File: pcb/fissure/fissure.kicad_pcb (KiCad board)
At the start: 2 copper layers, 99.5 x 95 mm, 45 parts, among them J1 AudioJack4, J2 AudioJack4, K1 KEYSW, K10 KEYSW, K11 KEYSW, K12 KEYSW, K13 KEYSW, K14 KEYSW, K15 KEYSW, K16 KEYSW, K17 KEYSW, K18 KEYSW, K2 KEYSW, K3 KEYSW, K4 KEYSW, K5 KEYSW, K6 KEYSW, K7 KEYSW, K8 KEYSW, K9 KEYSW, SW1 SW_PUSH, U1 NRF24L01_Breakout, U3 ProMicro

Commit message: v2.1 final
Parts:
- removed U1: NRF24L01_Breakout, Connector_PinHeader_2.54mm:PinHeader_2x04_P2.54mm_Vertical
- added J3: joystick, footprints:joystick, B.Cu at (102.5, 120.2)
- added J4: joystick, footprints:joystick, F.Cu at (102.5, 120.2)
- J1, J2: footprint Keebio-Parts:TRRS-PJ-320A -> Keebio-Parts:TRRS-PJ-320D
- moved R2 72.9 mm to (59.5, 44.7), turned to 270 degrees
- moved R1 68.8 mm to (62.5, 44.7), turned to 270 degrees
- moved D15 9.71 mm to (96.5, 53.2)
- moved D14 9.31 mm to (88.5, 53.2)
- moved D17 7.42 mm to (92.5, 53.2)
- moved SW1 6.75 mm to (113.0, 54.2)
- moved D18 5.82 mm to (102.5, 53.2)
- moved D10 5.62 mm to (98.5, 53.2)
- moved D9 5.22 mm to (90.5, 53.2)
- moved D16 5.02 mm to (86.5, 53.2)
- moved D13 4.93 mm to (84.5, 53.2)
- moved D8 4.83 mm to (82.5, 53.2)
- moved D3 4.73 mm to (80.5, 53.2)
- moved K1 2.50 mm to (51.5, 87.2)
- moved K11 2.50 mm to (54.5, 121.2)
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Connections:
- U3 pad 1: TX -> COL1
- U3 pad 10: COL4 -> ROW4
- U3 pad 11: COL5 -> X
- U3 pad 12: RGB -> Y
- U3 pad 13: CS -> RGB
- U3 pad 14: MOSI -> COL5
- U3 pad 15: MISO -> COL4
- U3 pad 16: SCLK -> COL3
- U3 pad 17: ROW4 -> Net-(U3-Pad17)
- U3 pad 18: ROW3 -> Net-(U3-Pad18)
- U3 pad 19: ROW2 -> Net-(U3-Pad19)
- U3 pad 2: RX -> COL2
- U3 pad 20: ROW1 -> Net-(U3-Pad20)
- U3 pad 7: COL1 -> ROW1
- U3 pad 8: COL2 -> ROW2
- U3 pad 9: COL3 -> ROW3
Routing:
- net Y: track 0.00 -> 76.7 mm
- net X: track 0.00 -> 73.6 mm
- net SCLK: track 69.9 -> 0.00 mm
- net MISO: track 63.2 -> 0.00 mm
- net MOSI: track 59.7 -> 0.00 mm
- net CS: track 59.7 -> 0.00 mm
- net ROW3: track 181.1 -> 130.7 mm
- net ROW4: track 169.8 -> 120.5 mm
- net ROW1: track 140.6 -> 95.0 mm
- net GND: track 176.4 -> 221.9 mm, vias 0 -> 1
- net ROW2: track 159.5 -> 115.0 mm
- net RGB: track 111.7 -> 131.6 mm, vias 2 -> 1
- net COL1: track 18.2 -> 7.83 mm
- net Net-(D16-Pad1): track 79.3 -> 88.7 mm
- net COL5: track 38.0 -> 29.5 mm
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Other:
- board size 99.5 x 95 mm -> 100 x 95 mm
- board text removed: "CE"
- board text removed: "CS"
- board text removed: "GND"
- board text removed: "IRQ"
- board text removed: "MI"
- board text removed: "MO"
- board text removed: "SCK"
- board text removed: "VCC"

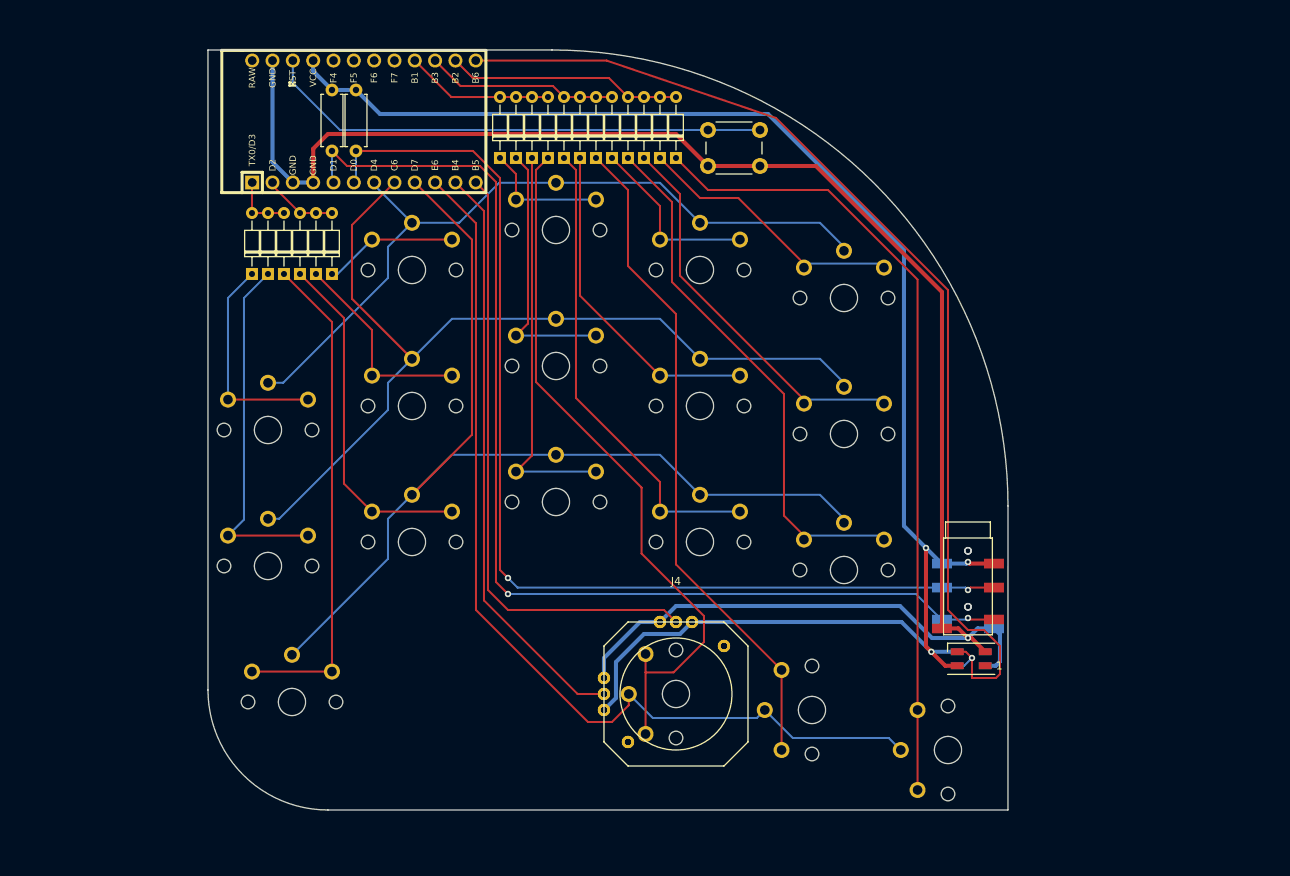
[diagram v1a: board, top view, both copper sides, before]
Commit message: New PCB version
- merge steno and split (no storage yet)
- experimental lower layer thumb cluster
- moved pro micro location
- SOD 123 diodes under switches
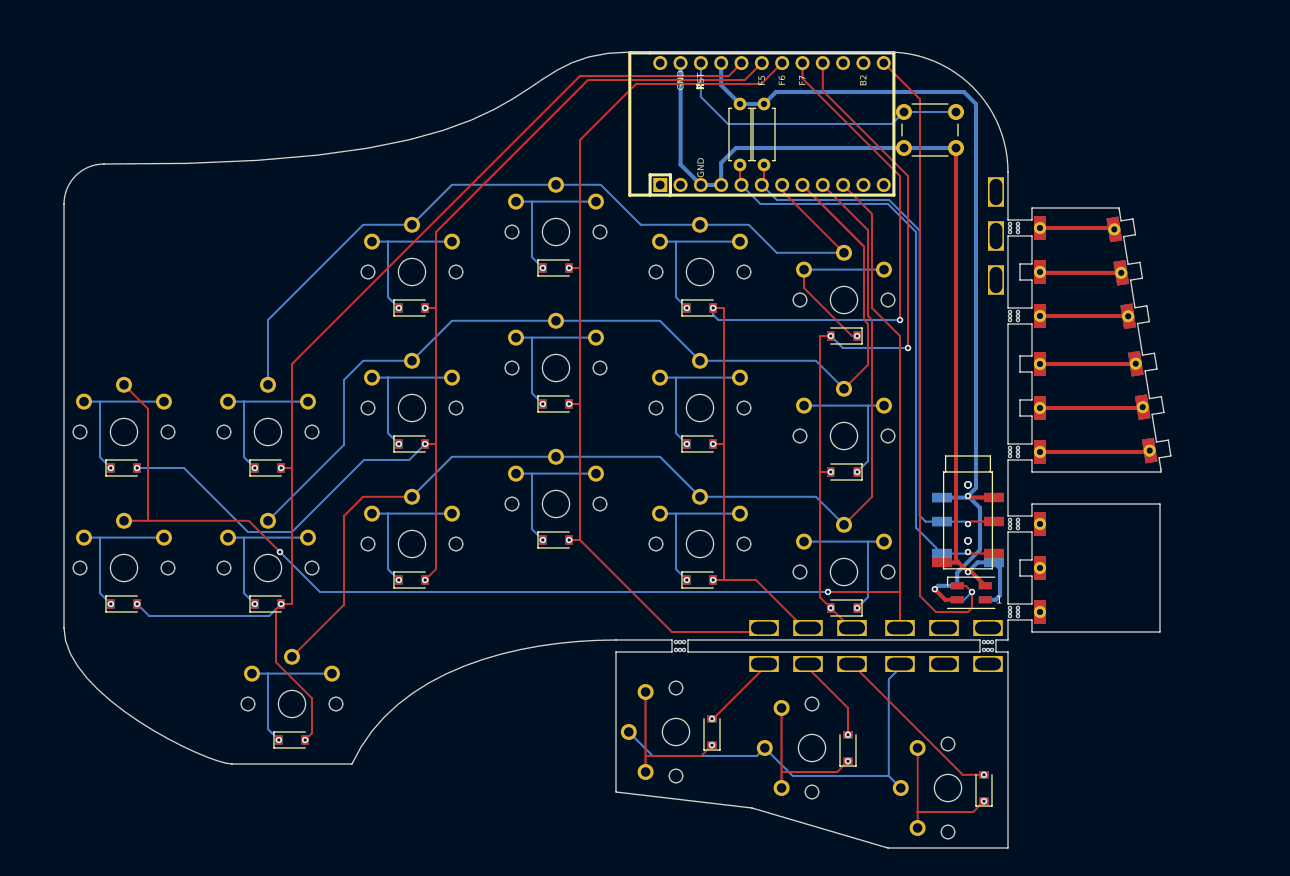
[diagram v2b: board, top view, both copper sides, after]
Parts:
- removed the D4 at (94.5, 53.2)
- removed the D6 at (51.5, 67.7)
- removed the K1 at (51.5, 87.2)
- added D1: DIODE, Diode_SMD:D_SOD-123, F.Cu at (51.5, 92.0)
- added D10: DIODE, Diode_SMD:D_SOD-123, B.Cu at (123.5, 75.5)
- added D11: DIODE, Diode_SMD:D_SOD-123, F.Cu at (51.5, 109.0)
- added D13: DIODE, Diode_SMD:D_SOD-123, F.Cu at (69.5, 89.0)
- added D15: DIODE, Diode_SMD:D_SOD-123, F.Cu at (87.5, 84.0)
- added D17: DIODE, Diode_SMD:D_SOD-123, F.Cu at (105.5, 89.0)
- added D19: DIODE, Diode_SMD:D_SOD-123, F.Cu at (123.5, 92.5)
- added D2: DIODE, Diode_SMD:D_SOD-123, B.Cu at (51.5, 92.0)
- added D21: DIODE, Diode_SMD:D_SOD-123, F.Cu at (54.5, 126.0)
- added D23: DIODE, Diode_SMD:D_SOD-123, F.Cu at (69.5, 106.0)
- added D25: DIODE, Diode_SMD:D_SOD-123, F.Cu at (87.5, 101.0)
- added D27: DIODE, Diode_SMD:D_SOD-123, F.Cu at (105.5, 106.0)
- added D29: DIODE, Diode_SMD:D_SOD-123, F.Cu at (123.5, 109.5)
- added D3: DIODE, Diode_SMD:D_SOD-123, F.Cu at (69.5, 72.0)
- added D31: DIODE, Diode_SMD:D_SOD-123, F.Cu at (33.5, 109.0)
- added D32: DIODE, Diode_SMD:D_SOD-123, B.Cu at (33.5, 109.0)
- added D33: DIODE, Diode_SMD:D_SOD-123, F.Cu at (33.5, 92.0)
- added D34: DIODE, Diode_SMD:D_SOD-123, B.Cu at (33.5, 92.0)
- added D35: DIODE, Diode_SMD:D_SOD-123, F.Cu at (107.0, 125.0)
- added D37: DIODE, Diode_SMD:D_SOD-123, F.Cu at (124.0, 127.0)
- added D39: DIODE, Diode_SMD:D_SOD-123, F.Cu at (141.0, 132.0)
- added D7: DIODE, Diode_SMD:D_SOD-123, F.Cu at (105.5, 72.0)
- added D8: DIODE, Diode_SMD:D_SOD-123, B.Cu at (105.5, 72.0)
- added D9: DIODE, Diode_SMD:D_SOD-123, F.Cu at (123.5, 75.5)
- added J5: Conn_01x03, fissure:feet, F.Cu at (148.0, 104.5)
- added J6: Conn_01x03, fissure:feet-conn, F.Cu at (142.5, 63.0)
- added J7: Conn_01x06, fissure:bridge, F.Cu at (148.0, 76.0)
- added J8: Conn_01x06, fissure:bridge, F.Cu at (159.5, 76.0)
- added K11: KEYSW, Keebio-Parts:Kailh-PG1350-1u-reversible-No-Clickhole, F.Cu at (54.5, 121.5)
- added K16: KEYSW, Keebio-Parts:Kailh-PG1350-1u-reversible-No-Clickhole, F.Cu at (33.5, 104.5)
- added K19: KEYSW, Keebio-Parts:Kailh-PG1350-1u-reversible-No-Clickhole, F.Cu at (119.5, 127.0)
- added REF**: breakaway-hole, Keebio-Parts:breakaway-hole, F.Cu at (144.0, 99.0)
- added REF**: breakaway-hole, Keebio-Parts:breakaway-hole, F.Cu at (145.5, 62.0)
- added REF**: breakaway-hole, Keebio-Parts:breakaway-hole, F.Cu at (144.0, 73.0)
- added REF**: breakaway-hole, Keebio-Parts:breakaway-hole, F.Cu at (145.5, 73.0)
- added REF**: breakaway-hole, Keebio-Parts:breakaway-hole, F.Cu at (144.0, 90.0)
- added REF**: breakaway-hole, Keebio-Parts:breakaway-hole, F.Cu at (145.5, 90.0)
- added REF**: breakaway-hole, Keebio-Parts:breakaway-hole, F.Cu at (103.5, 113.5)
- added REF**: breakaway-hole, Keebio-Parts:breakaway-hole, F.Cu at (102.5, 115.0)
- added REF**: breakaway-hole, Keebio-Parts:breakaway-hole, F.Cu at (102.5, 113.5)
- added REF**: breakaway-hole, Keebio-Parts:breakaway-hole, F.Cu at (103.5, 115.0)
- added REF**: breakaway-hole, Keebio-Parts:breakaway-hole, F.Cu at (142.0, 113.5)
- added REF**: breakaway-hole, Keebio-Parts:breakaway-hole, F.Cu at (145.5, 99.0)
- added REF**: breakaway-hole, Keebio-Parts:breakaway-hole, F.Cu at (141.0, 115.0)
- added REF**: breakaway-hole, Keebio-Parts:breakaway-hole, F.Cu at (141.0, 113.5)
- added REF**: breakaway-hole, Keebio-Parts:breakaway-hole, F.Cu at (142.0, 115.0)
- added REF**: breakaway-hole, Keebio-Parts:breakaway-hole, F.Cu at (145.5, 110.5)
- added REF**: breakaway-hole, Keebio-Parts:breakaway-hole, F.Cu at (144.0, 109.5)
- added REF**: breakaway-hole, Keebio-Parts:breakaway-hole, F.Cu at (145.5, 109.5)
- added REF**: breakaway-hole, Keebio-Parts:breakaway-hole, F.Cu at (144.0, 110.5)
- added REF**: breakaway-hole, Keebio-Parts:breakaway-hole, F.Cu at (144.0, 98.5)
- added REF**: breakaway-hole, Keebio-Parts:breakaway-hole, F.Cu at (145.5, 99.5)
- added REF**: breakaway-hole, Keebio-Parts:breakaway-hole, F.Cu at (144.0, 99.5)
- added REF**: breakaway-hole, Keebio-Parts:breakaway-hole, F.Cu at (144.0, 110.0)
- added REF**: breakaway-hole, Keebio-Parts:breakaway-hole, F.Cu at (145.5, 98.5)
- added REF**: breakaway-hole, Keebio-Parts:breakaway-hole, F.Cu at (145.5, 62.5)
- added REF**: breakaway-hole, Keebio-Parts:breakaway-hole, F.Cu at (144.0, 61.5)
- added REF**: breakaway-hole, Keebio-Parts:breakaway-hole, F.Cu at (145.5, 61.5)
- added REF**: breakaway-hole, Keebio-Parts:breakaway-hole, F.Cu at (144.0, 62.5)
- added REF**: breakaway-hole, Keebio-Parts:breakaway-hole, F.Cu at (145.5, 73.5)
- added REF**: breakaway-hole, Keebio-Parts:breakaway-hole, F.Cu at (144.0, 72.5)
- added REF**: breakaway-hole, Keebio-Parts:breakaway-hole, F.Cu at (145.5, 72.5)
- added REF**: breakaway-hole, Keebio-Parts:breakaway-hole, F.Cu at (144.0, 73.5)
- added REF**: breakaway-hole, Keebio-Parts:breakaway-hole, F.Cu at (144.0, 89.5)
- added REF**: breakaway-hole, Keebio-Parts:breakaway-hole, F.Cu at (145.5, 110.0)
- added REF**: breakaway-hole, Keebio-Parts:breakaway-hole, F.Cu at (144.0, 90.5)
- added REF**: breakaway-hole, Keebio-Parts:breakaway-hole, F.Cu at (145.5, 89.5)
- added REF**: breakaway-hole, Keebio-Parts:breakaway-hole, F.Cu at (145.5, 90.5)
- added REF**: breakaway-hole, Keebio-Parts:breakaway-hole, F.Cu at (141.5, 113.5)
- added REF**: breakaway-hole, Keebio-Parts:breakaway-hole, F.Cu at (103.0, 113.5)
- added REF**: breakaway-hole, Keebio-Parts:breakaway-hole, F.Cu at (103.0, 115.0)
- added REF**: breakaway-hole, Keebio-Parts:breakaway-hole, F.Cu at (141.5, 115.0)
- added REF**: breakaway-hole, Keebio-Parts:breakaway-hole, F.Cu at (144.0, 62.0)
- D12: renamed from D11; footprint Diode_THT:D_DO-34_SOD68_P7.62mm_Horizontal -> Diode_SMD:D_SOD-123; moved to B.Cu
- D14: renamed from D7; footprint Diode_THT:D_DO-34_SOD68_P7.62mm_Horizontal -> Diode_SMD:D_SOD-123; moved to B.Cu
- D16: renamed from D8; footprint Diode_THT:D_DO-34_SOD68_P7.62mm_Horizontal -> Diode_SMD:D_SOD-123; moved to B.Cu
- D18: renamed from D9; footprint Diode_THT:D_DO-34_SOD68_P7.62mm_Horizontal -> Diode_SMD:D_SOD-123; moved to B.Cu
- D20: renamed from D10; footprint Diode_THT:D_DO-34_SOD68_P7.62mm_Horizontal -> Diode_SMD:D_SOD-123; moved to B.Cu
- D22: renamed from D1; footprint Diode_THT:D_DO-34_SOD68_P7.62mm_Horizontal -> Diode_SMD:D_SOD-123; moved to B.Cu
- D24: renamed from D12; footprint Diode_THT:D_DO-34_SOD68_P7.62mm_Horizontal -> Diode_SMD:D_SOD-123; moved to B.Cu
- D26: renamed from D13; footprint Diode_THT:D_DO-34_SOD68_P7.62mm_Horizontal -> Diode_SMD:D_SOD-123; moved to B.Cu
- D28: renamed from D14; footprint Diode_THT:D_DO-34_SOD68_P7.62mm_Horizontal -> Diode_SMD:D_SOD-123; moved to B.Cu
- D30: renamed from D15; footprint Diode_THT:D_DO-34_SOD68_P7.62mm_Horizontal -> Diode_SMD:D_SOD-123; moved to B.Cu
- D36: renamed from D16; footprint Diode_THT:D_DO-34_SOD68_P7.62mm_Horizontal -> Diode_SMD:D_SOD-123; moved to B.Cu
- D38: renamed from D17; footprint Diode_THT:D_DO-34_SOD68_P7.62mm_Horizontal -> Diode_SMD:D_SOD-123; moved to B.Cu
- D4: renamed from D2; footprint Diode_THT:D_DO-34_SOD68_P7.62mm_Horizontal -> Diode_SMD:D_SOD-123; moved to B.Cu
- D40: renamed from D18; footprint Diode_THT:D_DO-34_SOD68_P7.62mm_Horizontal -> Diode_SMD:D_SOD-123; moved to B.Cu
- D5: footprint Diode_THT:D_DO-34_SOD68_P7.62mm_Horizontal -> Diode_SMD:D_SOD-123
- D6: renamed from D3; footprint Diode_THT:D_DO-34_SOD68_P7.62mm_Horizontal -> Diode_SMD:D_SOD-123; moved to B.Cu
- J3: value joystick -> Conn_01x06; footprint footprints:joystick -> fissure:bridge-conn; moved to F.Cu
- J4: value joystick -> Conn_01x06; footprint footprints:joystick -> fissure:bridge-conn
- moved K17 92.8 mm to (33.5, 87.5), turned to 180 degrees
- moved D40 87.7 mm to (141.0, 132.0)
- moved D38 80.2 mm to (124.0, 127.0)
- moved D36 74.6 mm to (107.0, 125.0)
- moved D30 62.4 mm to (123.5, 109.5), turned to 180 degrees
- moved D22 58.5 mm to (54.5, 126.0), turned to 0 degrees
- moved D28 55.4 mm to (105.5, 106.0), turned to 0 degrees
- moved R1 51.0 mm to (113.5, 46.5)
- moved R2 51.0 mm to (110.5, 46.5)
- moved U1 51.0 mm to (114.5, 49.0)
- moved D26 47.8 mm to (87.5, 101.0), turned to 0 degrees
- moved D20 46.5 mm to (123.5, 92.5), turned to 180 degrees
- moved D12 41.3 mm to (51.5, 109.0), turned to 0 degrees
- moved D24 40.7 mm to (69.5, 106.0), turned to 0 degrees
- moved D18 38.8 mm to (105.5, 89.0), turned to 0 degrees
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- renumbered D20 to D41, D21 to D42, K6 to K1, K16 to K18, K18 to K20, K11 to K6, U3 to U1
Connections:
- D36 pad 2: COL3 -> Net-(D35-Pad2)
- D38 pad 1: Net-(D17-Pad1) (its old number) -> Net-(D37-Pad1)
- D38 pad 2: COL4 -> Net-(D37-Pad2)
- D40 pad 2: COL5 -> Net-(D39-Pad2)
- D5 pad 2: COL5 -> COL3
- D6 pad 1: Net-(D3-Pad1) (its old number) -> Net-(D5-Pad1)
- J3 pad 1: VCC -> COL3
- J3 pad 2: Y -> COL4
- J3 pad 3: GND -> COL5
- J3 pad 4: GND -> ROW4
- J3 pad 5: X -> Net-(J3-Pad5)
- J3 pad 6: VCC -> Net-(J3-Pad6)
- J4 pad 1: VCC -> Net-(D35-Pad2)
- J4 pad 2: X -> Net-(D37-Pad2)
- J4 pad 3: GND -> Net-(D39-Pad2)
- J4 pad 4: GND -> Net-(J4-Pad4)
- J4 pad 5: Y -> Net-(J4-Pad5)
- J4 pad 6: VCC -> Net-(J4-Pad6)
- K1 pad 1: ROW2 -> ROW1
- K17 pad 2: Net-(D17-Pad1) (its old number) -> Net-(D33-Pad1)
- K18 pad 1: ROW4 -> Net-(J4-Pad4)
- K20 pad 1: ROW4 -> Net-(J4-Pad4)
- K3 pad 2: Net-(D3-Pad1) (its old number) -> Net-(D5-Pad1)
- K5 pad 2: Net-(D5-Pad1) -> Net-(D10-Pad1)
- K6 pad 1: ROW3 -> ROW2
- U1 pad 1: COL1 -> Net-(U1-Pad1)
- U1 pad 11: X -> Y
- U1 pad 12: Y -> X
- U1 pad 14: COL5 -> Net-(U1-Pad14)
- U1 pad 15: COL4 -> COL6
- U1 pad 16: COL3 -> COL5
- U1 pad 17: Net-(U3-Pad17) -> COL4
- U1 pad 18: Net-(U3-Pad18) -> COL3
- U1 pad 19: Net-(U3-Pad19) -> COL2
- U1 pad 2: COL2 -> Net-(U1-Pad2)
- U1 pad 20: Net-(U3-Pad20) -> COL1
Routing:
- net COL1: track 7.83 -> 143.2 mm, vias 0 -> 4
- net COL2: track 9.24 -> 140.1 mm, vias 0 -> 4
- net GND: track 221.9 -> 120.5 mm
- net COL3: track 18.5 -> 111.1 mm, vias 0 -> 3
- net VCC: track 202.4 -> 112.3 mm, vias 3 -> 2
- net COL4: track 24.0 -> 112.9 mm, vias 0 -> 4
- net Net-(D17-Pad1) (its old number): track 83.6 -> 0.00 mm
- net Net-(D39-Pad1): track 100.3 -> 18.9 mm, vias 0 -> 1
- net Y: track 76.7 -> 0.00 mm
- net X: track 73.6 -> 0.00 mm
- net Net-(D35-Pad1): track 88.7 -> 18.9 mm, vias 0 -> 1
- net SCL: track 140.5 -> 75.0 mm, vias 2 -> 1
- net SDA: track 135.4 -> 70.2 mm, vias 2 -> 1
- net COL5: track 29.5 -> 91.8 mm, vias 0 -> 4
- net ROW4: track 120.5 -> 177.8 mm, vias 0 -> 2
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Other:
- board size 100 x 95 mm -> 138.4 x 99.5 mm

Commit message: PCB fixes
- move promicro to left edge, point USB port to top
- move TRRS jack to top, facing right
- move RGB to right side of T (on QWERTY)
- cut right side
- add OLED to top
- add QSPI flash to left
- cut thumb connections to 4
- make mousebite tabs 4mm wide from 2mm
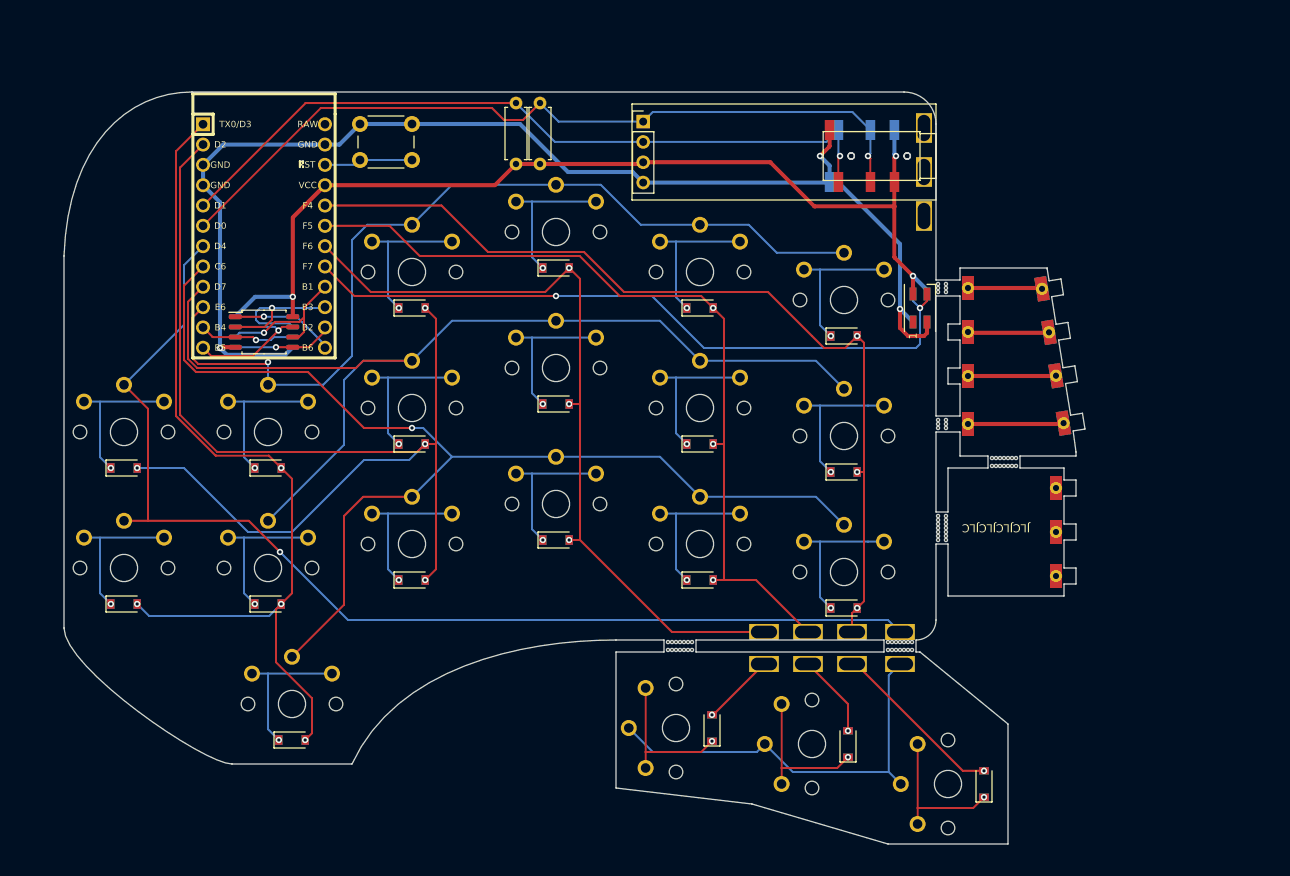
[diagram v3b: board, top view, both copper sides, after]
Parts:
- removed the REF** at (144.0, 99.0)
- removed the REF** at (145.5, 62.0)
- removed the REF** at (144.0, 73.0)
- removed the REF** at (145.5, 73.0)
- removed the REF** at (144.0, 90.0)
- removed the REF** at (145.5, 90.0)
- removed the REF** at (142.0, 113.5)
- removed the REF** at (145.5, 99.0)
- removed the REF** at (141.0, 115.0)
- removed the REF** at (141.0, 113.5)
- removed the REF** at (142.0, 115.0)
- removed the REF** at (145.5, 110.5)
- removed the REF** at (144.0, 109.5)
- removed the REF** at (145.5, 109.5)
- removed the REF** at (144.0, 110.5)
- removed the REF** at (144.0, 98.5)
- removed the REF** at (145.5, 99.5)
- removed the REF** at (144.0, 99.5)
- removed the REF** at (144.0, 110.0)
- removed the REF** at (145.5, 98.5)
- removed the REF** at (145.5, 62.5)
- removed the REF** at (144.0, 61.5)
- removed the REF** at (145.5, 61.5)
- removed the REF** at (144.0, 62.5)
- removed the REF** at (145.5, 73.5)
- removed the REF** at (144.0, 72.5)
- removed the REF** at (145.5, 72.5)
- removed the REF** at (144.0, 73.5)
- removed the REF** at (145.5, 110.0)
- removed the REF** at (145.5, 89.5)
- removed the REF** at (141.5, 113.5)
- removed the REF** at (141.5, 115.0)
- removed the REF** at (144.0, 62.0)
- added J9: Conn_01x04, steno:OLED, F.Cu at (97.0, 46.5)
- added REF**: breakaway-hole, Keebio-Parts:breakaway-hole, F.Cu at (143.0, 90.5)
- added REF**: breakaway-hole, Keebio-Parts:breakaway-hole, F.Cu at (142.0, 92.0)
- added REF**: breakaway-hole, Keebio-Parts:breakaway-hole, F.Cu at (142.5, 92.0)
- added REF**: breakaway-hole, Keebio-Parts:breakaway-hole, F.Cu at (145.0, 92.0)
- added REF**: breakaway-hole, Keebio-Parts:breakaway-hole, F.Cu at (143.5, 92.0)
- added REF**: breakaway-hole, Keebio-Parts:breakaway-hole, F.Cu at (144.5, 92.0)
- added REF**: breakaway-hole, Keebio-Parts:breakaway-hole, F.Cu at (136.5, 99.0)
- added REF**: breakaway-hole, Keebio-Parts:breakaway-hole, F.Cu at (136.5, 100.0)
- added REF**: breakaway-hole, Keebio-Parts:breakaway-hole, F.Cu at (136.5, 101.0)
- added REF**: breakaway-hole, Keebio-Parts:breakaway-hole, F.Cu at (136.5, 100.5)
- added REF**: breakaway-hole, Keebio-Parts:breakaway-hole, F.Cu at (136.5, 98.0)
- added REF**: breakaway-hole, Keebio-Parts:breakaway-hole, F.Cu at (136.5, 99.5)
- added REF**: breakaway-hole, Keebio-Parts:breakaway-hole, F.Cu at (136.5, 98.5)
- added REF**: breakaway-hole, Keebio-Parts:breakaway-hole, F.Cu at (135.0, 100.0)
- added REF**: breakaway-hole, Keebio-Parts:breakaway-hole, F.Cu at (135.0, 99.0)
- added REF**: breakaway-hole, Keebio-Parts:breakaway-hole, F.Cu at (135.0, 98.0)
- added REF**: breakaway-hole, Keebio-Parts:breakaway-hole, F.Cu at (135.0, 98.5)
- added REF**: breakaway-hole, Keebio-Parts:breakaway-hole, F.Cu at (135.0, 101.0)
- added REF**: breakaway-hole, Keebio-Parts:breakaway-hole, F.Cu at (135.0, 99.5)
- added REF**: breakaway-hole, Keebio-Parts:breakaway-hole, F.Cu at (135.0, 100.5)
- added REF**: breakaway-hole, Keebio-Parts:breakaway-hole, F.Cu at (131.0, 115.0)
- added REF**: breakaway-hole, Keebio-Parts:breakaway-hole, F.Cu at (145.0, 90.5)
- added REF**: breakaway-hole, Keebio-Parts:breakaway-hole, F.Cu at (130.0, 115.0)
- added REF**: breakaway-hole, Keebio-Parts:breakaway-hole, F.Cu at (129.0, 115.0)
- added REF**: breakaway-hole, Keebio-Parts:breakaway-hole, F.Cu at (129.5, 115.0)
- added REF**: breakaway-hole, Keebio-Parts:breakaway-hole, F.Cu at (132.0, 115.0)
- added REF**: breakaway-hole, Keebio-Parts:breakaway-hole, F.Cu at (130.5, 115.0)
- added REF**: breakaway-hole, Keebio-Parts:breakaway-hole, F.Cu at (131.5, 115.0)
- added REF**: breakaway-hole, Keebio-Parts:breakaway-hole, F.Cu at (130.0, 113.5)
- added REF**: breakaway-hole, Keebio-Parts:breakaway-hole, F.Cu at (131.0, 113.5)
- added REF**: breakaway-hole, Keebio-Parts:breakaway-hole, F.Cu at (132.0, 113.5)
- added REF**: breakaway-hole, Keebio-Parts:breakaway-hole, F.Cu at (131.5, 113.5)
- added REF**: breakaway-hole, Keebio-Parts:breakaway-hole, F.Cu at (144.5, 90.5)
- added REF**: breakaway-hole, Keebio-Parts:breakaway-hole, F.Cu at (129.0, 113.5)
- added REF**: breakaway-hole, Keebio-Parts:breakaway-hole, F.Cu at (130.5, 113.5)
- added REF**: breakaway-hole, Keebio-Parts:breakaway-hole, F.Cu at (129.5, 113.5)
- added REF**: breakaway-hole, Keebio-Parts:breakaway-hole, F.Cu at (101.5, 115.0)
- added REF**: breakaway-hole, Keebio-Parts:breakaway-hole, F.Cu at (102.0, 115.0)
- added REF**: breakaway-hole, Keebio-Parts:breakaway-hole, F.Cu at (104.5, 115.0)
- added REF**: breakaway-hole, Keebio-Parts:breakaway-hole, F.Cu at (104.0, 115.0)
- added REF**: breakaway-hole, Keebio-Parts:breakaway-hole, F.Cu at (142.0, 90.5)
- added REF**: breakaway-hole, Keebio-Parts:breakaway-hole, F.Cu at (104.0, 113.5)
- added REF**: breakaway-hole, Keebio-Parts:breakaway-hole, F.Cu at (102.0, 113.5)
- added REF**: breakaway-hole, Keebio-Parts:breakaway-hole, F.Cu at (104.5, 113.5)
- added REF**: breakaway-hole, Keebio-Parts:breakaway-hole, F.Cu at (101.5, 113.5)
- added REF**: breakaway-hole, Keebio-Parts:breakaway-hole, F.Cu at (135.0, 69.5)
- added REF**: breakaway-hole, Keebio-Parts:breakaway-hole, F.Cu at (136.5, 69.5)
- added REF**: breakaway-hole, Keebio-Parts:breakaway-hole, F.Cu at (135.0, 86.5)
- added REF**: breakaway-hole, Keebio-Parts:breakaway-hole, F.Cu at (136.5, 86.5)
- added REF**: breakaway-hole, Keebio-Parts:breakaway-hole, F.Cu at (143.5, 90.5)
- added REF**: breakaway-hole, Keebio-Parts:breakaway-hole, F.Cu at (136.5, 70.0)
- added REF**: breakaway-hole, Keebio-Parts:breakaway-hole, F.Cu at (135.0, 69.0)
- added REF**: breakaway-hole, Keebio-Parts:breakaway-hole, F.Cu at (136.5, 69.0)
- added REF**: breakaway-hole, Keebio-Parts:breakaway-hole, F.Cu at (135.0, 70.0)
- added REF**: breakaway-hole, Keebio-Parts:breakaway-hole, F.Cu at (135.0, 87.0)
- added REF**: breakaway-hole, Keebio-Parts:breakaway-hole, F.Cu at (136.5, 86.0)
- added REF**: breakaway-hole, Keebio-Parts:breakaway-hole, F.Cu at (142.5, 90.5)
- added REF**: breakaway-hole, Keebio-Parts:breakaway-hole, F.Cu at (144.0, 92.0)
- added REF**: breakaway-hole, Keebio-Parts:breakaway-hole, F.Cu at (143.0, 92.0)
- added U2: MT25QL128ABA1ESE, Package_SO:SOP-8_5.28x5.23mm_P1.27mm, F.Cu at (51.0, 75.0)
- added U3: MT25QL128ABA1ESE, Package_SO:SOP-8_5.28x5.23mm_P1.27mm, B.Cu at (51.0, 75.0)
- J3, J4, J7, J8: value Conn_01x06 -> Conn_01x04
- moved SW1 74.6 mm to (63.0, 49.0), turned to 0 degrees
- moved U1 65.0 mm to (51.0, 63.0), turned to 270 degrees
- moved J1 40.0 mm to (133.0, 53.0), turned to 270 degrees
- moved J2 40.0 mm to (133.0, 53.0), turned to 90 degrees
- moved D41 36.2 mm to (133.0, 72.0), turned to 90 degrees
- moved D42 36.2 mm to (133.0, 72.0), turned to 90 degrees
- moved R1 29.0 mm to (85.5, 54.0), turned to 90 degrees
- moved R2 29.0 mm to (82.5, 54.0), turned to 90 degrees
- moved J6 12.0 mm to (133.5, 55.0)
- moved J8 10.1 mm to (149.6, 78.0)
- moved REF** 9.66 mm to (135.0, 86.0)
- moved REF** 9.66 mm to (136.5, 87.0)
- moved J7 9.22 mm to (139.0, 78.0)
- moved J3 6.02 mm to (121.5, 112.5)
- moved J4 6.00 mm to (121.5, 116.5)
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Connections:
- U1 pad 1: Net-(U1-Pad1) -> COL1
- U1 pad 10: ROW4 -> ROW1
- U1 pad 11: Y -> DQ2
- U1 pad 12: X -> DQ3
- U1 pad 13: RGB -> CS
- U1 pad 14: Net-(U1-Pad14) -> MOSI_DQ0
- U1 pad 15: COL6 -> MISO_DQ1
- U1 pad 16: COL5 -> SCLK
- U1 pad 17: COL4 -> RGB
- U1 pad 19: COL2 -> COL4
- U1 pad 2: Net-(U1-Pad2) -> COL2
- U1 pad 20: COL1 -> COL5
- U1 pad 7: ROW1 -> ROW4
- U1 pad 8: ROW2 -> ROW3
- U1 pad 9: ROW3 -> ROW2
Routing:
- net GND: track 120.5 -> 156.7 mm, vias 1 -> 3
- net ROW4: track 177.8 -> 142.4 mm, vias 2 -> 1
- net COL1: track 143.2 -> 110.6 mm
- net SDA: track 70.2 -> 100.2 mm
- net RST: track 38.1 -> 11.1 mm
- net COL5: track 91.8 -> 113.4 mm, vias 4 -> 3
- net MISO_DQ1: track 0.00 -> 21.3 mm, vias 0 -> 1
- net SCL: track 75.0 -> 94.0 mm
- net DQ3: track 0.00 -> 18.7 mm, vias 0 -> 1
- net SCLK: track 0.00 -> 18.0 mm, vias 0 -> 1
- net Net-(J7-Pad6): track 13.8 -> 0.00 mm
- net VCC: track 112.3 -> 125.6 mm, vias 2 -> 3
- net CS: track 0.00 -> 13.0 mm, vias 0 -> 1
- net Net-(J7-Pad5): track 12.9 -> 0.00 mm
- net MOSI_DQ0: track 0.00 -> 12.5 mm, vias 0 -> 1
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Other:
- board size 138.4 x 99.5 mm -> 127.6 x 94 mm
- board text added: "JLCJLCJLCJLC"
